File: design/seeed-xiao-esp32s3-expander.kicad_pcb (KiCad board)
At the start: 2 copper layers, 17.8 x 21.4 mm, 15 parts, among them J1 Header 1x7 2.54mm, J2 Header 1x7 2.54mm, J3 30pin, K1 TS-1185E, U1 Wio-SX1262

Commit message: Update pcb from schematic
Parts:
- removed C1: 100nF, Capacitor:C0402
- removed D1: Green, Diode:LED-0603
- removed J2: Header 1x7 2.54mm, Connector:H7-2.54
- removed K1: TS-1185E, Switch:BUTTON2P_3_9X3X2MM
- removed R1, R3: 10K, Resistor:R0402
- removed R2: 330R, Resistor:R0402
- removed R4, R5, R6, R7: 47R, Resistor:R0402
- removed TP1: Test Point, Misc:TP-D3_5c2_2mm
- removed U1: Wio-SX1262, Module:MODULE12P-1.27-11X11.6MM
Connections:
- J1 pad 1: LORA_DIO1 -> GPIO14
- J1 pad 2: LORA_BUSY -> GPIO15
- J1 pad 3: LORA_RST -> GPIO16
- J1 pad 4: LORA_SPI_NSS -> GPIO17
- J1 pad 5: LORA_RF_SW1 -> GPIO18
- J1 pad 6: unconnected-(J1-Pad6) -> GPIO47
- J1 pad 7: unconnected-(J1-Pad7) -> GPIO48
- J3 pad 10: LORA_SPI_MOSI -> unconnected-(J3-Pad10)
- J3 pad 11: LORA_BUSY -> unconnected-(J3-Pad11)
- J3 pad 13: LORA_DIO1 -> unconnected-(J3-Pad13)
- J3 pad 15: LORA_RF_SW1 -> unconnected-(J3-Pad15)
- J3 pad 6: LORA_SPI_SCK -> unconnected-(J3-Pad6)
- J3 pad 7: LORA_RST -> unconnected-(J3-Pad7)
- J3 pad 8: LORA_SPI_MISO -> unconnected-(J3-Pad8)
- J3 pad 9: LORA_SPI_NSS -> unconnected-(J3-Pad9)
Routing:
- net (no net): track 0.00 -> 136.0 mm, vias 0 -> 4
- net LORA_RST: track 29.9 -> 0.00 mm, vias 2 -> 0
- net LORA_DIO1: track 25.5 -> 0.00 mm, vias 1 -> 0
- net unconnected-(J3-Pad8): track 0.00 -> 23.6 mm, vias 0 -> 1
- net LORA_SPI_MISO: track 23.6 -> 0.00 mm, vias 1 -> 0
- net LORA_BUSY: track 23.2 -> 0.00 mm, vias 1 -> 0
- net unconnected-(J3-Pad10): track 0.00 -> 20.6 mm, vias 0 -> 1
- net LORA_SPI_MOSI: track 20.6 -> 0.00 mm, vias 1 -> 0
- net unconnected-(J3-Pad6): track 0.00 -> 20.4 mm, vias 0 -> 2
- net LORA_SPI_SCK: track 20.4 -> 0.00 mm, vias 2 -> 0
- net LORA_SPI_NSS: track 19.7 -> 0.00 mm, vias 3 -> 0
- net LORA_RF_SW1: track 19.2 -> 0.00 mm, vias 1 -> 0
- net Net-(U1-NSS): track 4.43 -> 0.00 mm, vias 1 -> 0
- net Net-(U1-MISO): track 4.33 -> 0.00 mm, vias 1 -> 0
- net Net-(U1-MOSI): track 4.27 -> 0.00 mm, vias 1 -> 0
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
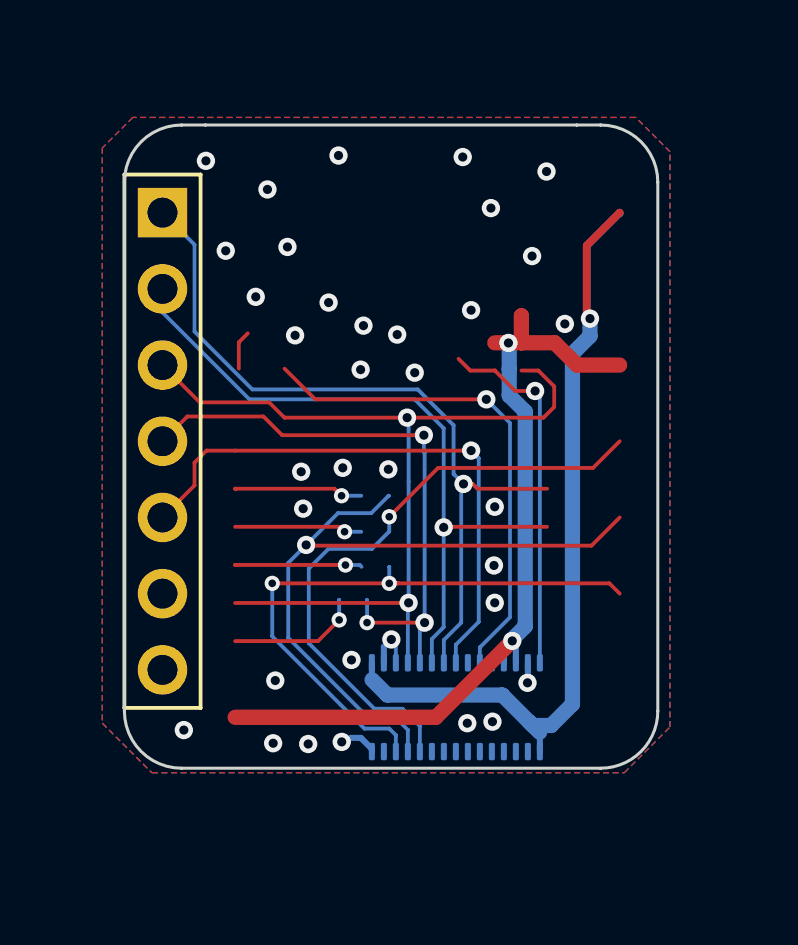
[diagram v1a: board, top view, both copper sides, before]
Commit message: Clean up traces and vias
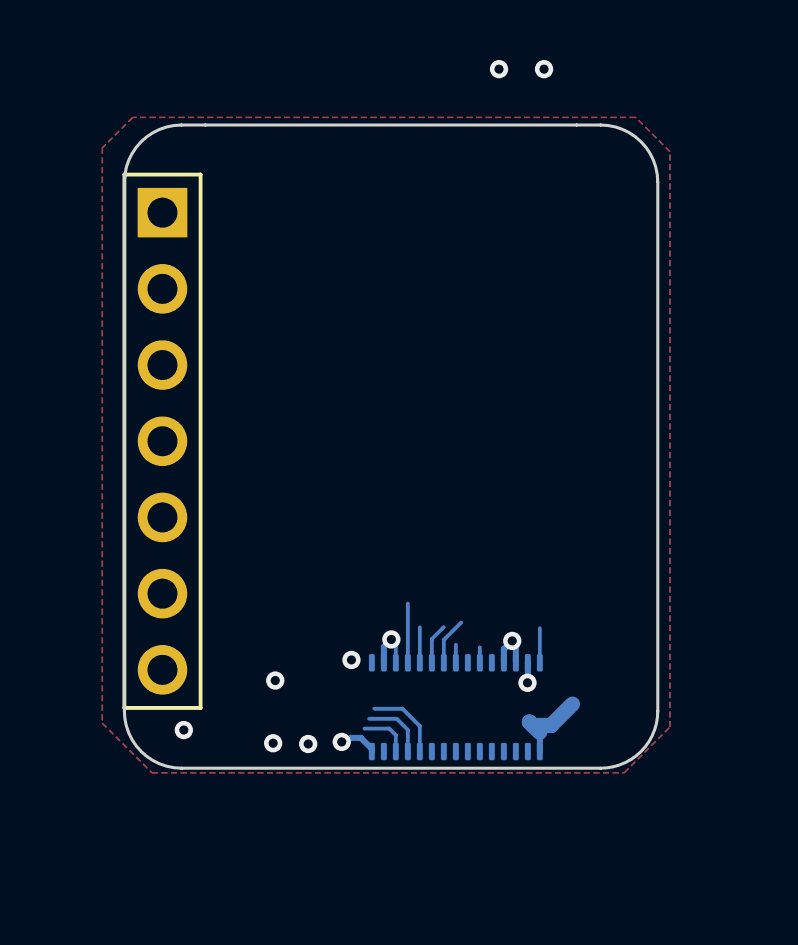
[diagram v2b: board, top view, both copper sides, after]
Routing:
- net (no net): track 136.0 -> 0.00 mm, vias 4 -> 0
- net VIN: track 30.5 -> 2.91 mm, vias 1 -> 0
- net +3V3: track 27.6 -> 1.62 mm, vias 2 -> 1
- net unconnected-(J3-Pad8): track 23.6 -> 2.17 mm, vias 1 -> 0
- net unconnected-(J3-Pad6): track 20.4 -> 1.68 mm, vias 2 -> 0
- net unconnected-(J3-Pad10): track 20.6 -> 2.61 mm, vias 1 -> 0
- net GPIO48: track 16.7 -> 0.51 mm, vias 1 -> 0
- net GPIO21: track 12.1 -> 1.15 mm, vias 1 -> 0
- net unconnected-(J3-Pad7): track 0.00 -> 1.97 mm, vias 2 -> 0
- net unconnected-(J3-Pad13): track 0.00 -> 1.58 mm, vias 1 -> 0
- net unconnected-(J3-Pad11): track 0.00 -> 1.35 mm, vias 1 -> 0
- net unconnected-(J3-Pad9): track 0.00 -> 1.18 mm, vias 3 -> 0
- net unconnected-(J3-Pad15): track 0.00 -> 0.60 mm, vias 1 -> 0
- net GND: vias 35 -> 10

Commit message: Arrange breakout holes and pads
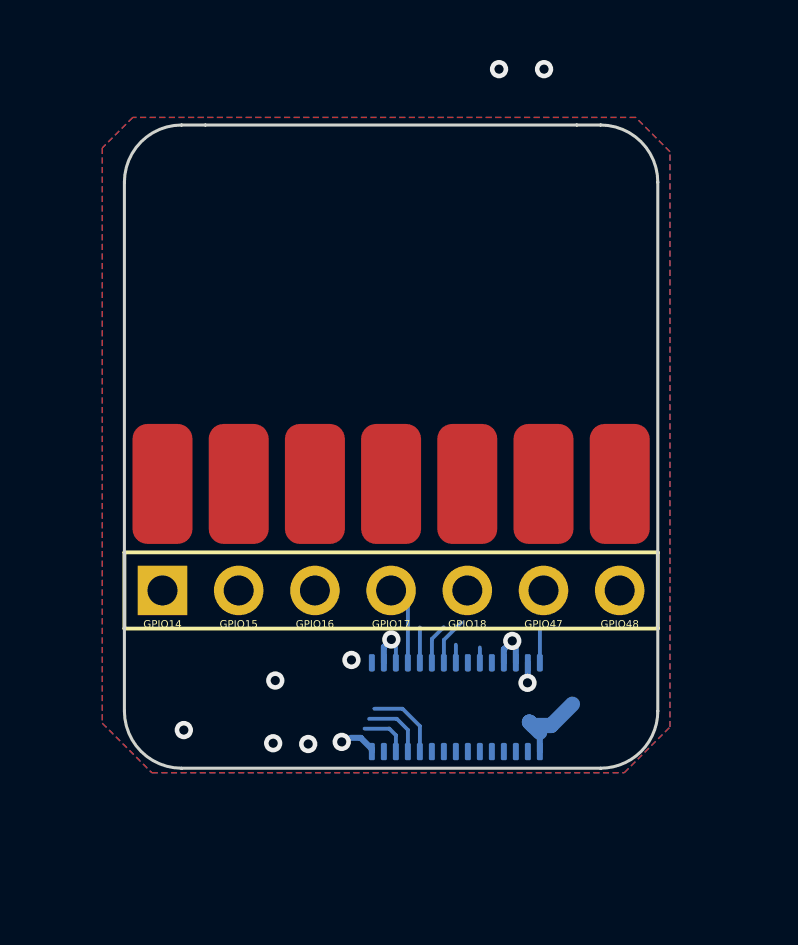
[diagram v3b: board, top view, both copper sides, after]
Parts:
- added GPIO14: SolderWirePad_1x01_SMD_2x4mm, Connector_Wire:SolderWirePad_1x01_SMD_2x4mm, F.Cu at (106.8, 122.3)
- added GPIO15: SolderWirePad_1x01_SMD_2x4mm, Connector_Wire:SolderWirePad_1x01_SMD_2x4mm, F.Cu at (109.3, 122.3)
- added GPIO16: SolderWirePad_1x01_SMD_2x4mm, Connector_Wire:SolderWirePad_1x01_SMD_2x4mm, F.Cu at (111.9, 122.3)
- added GPIO17: SolderWirePad_1x01_SMD_2x4mm, Connector_Wire:SolderWirePad_1x01_SMD_2x4mm, F.Cu at (114.4, 122.3)
- added GPIO18: SolderWirePad_1x01_SMD_2x4mm, Connector_Wire:SolderWirePad_1x01_SMD_2x4mm, F.Cu at (116.9, 122.3)
- added GPIO47: SolderWirePad_1x01_SMD_2x4mm, Connector_Wire:SolderWirePad_1x01_SMD_2x4mm, F.Cu at (119.5, 122.3)
- added GPIO48: SolderWirePad_1x01_SMD_2x4mm, Connector_Wire:SolderWirePad_1x01_SMD_2x4mm, F.Cu at (122.0, 122.3)
- moved J1 9.10 mm to (114.4, 125.9), turned to 90 degrees

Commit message: Add shared footprint for solder pad
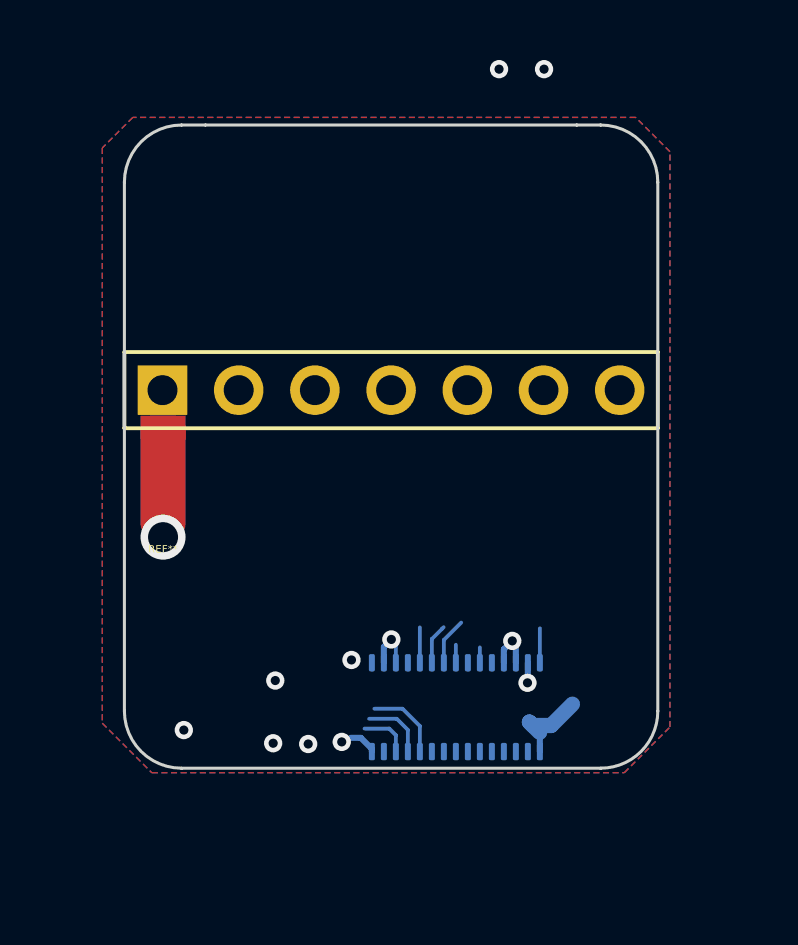
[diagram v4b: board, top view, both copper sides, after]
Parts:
- removed GPIO14, GPIO15, GPIO16, GPIO17, GPIO18, GPIO47, GPIO48: SolderWirePad_1x01_SMD_2x4mm, Connector_Wire:SolderWirePad_1x01_SMD_2x4mm
- added REF**: SolderPad_1x01_SMD, seeed-xiao-esp32s3-expander:SolderPad_1x01_SMD, F.Cu at (106.8, 122.0)
- moved J1 6.68 mm to (114.4, 119.2)
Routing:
- net unconnected-(J3-Pad7): track 1.97 -> 0.00 mm
- net GPIO14: vias 0 -> 1

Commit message: Add more organized header pad combo
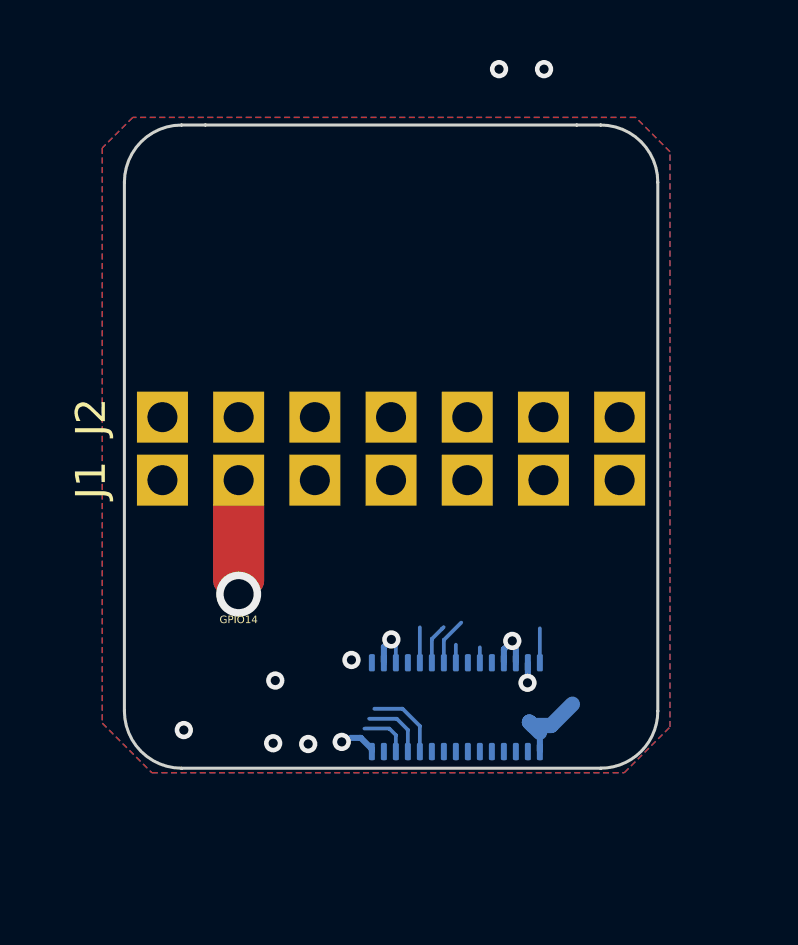
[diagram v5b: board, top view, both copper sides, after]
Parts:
- removed REF**: SolderPad_1x01_SMD, seeed-xiao-esp32s3-expander:SolderPad_1x01_SMD
- added GPIO14: SolderPad_1x01_SMD, seeed-xiao-esp32s3-expander:SolderPad_1x01_SMD, F.Cu at (109.3, 124.7)
- added J2: Conn_01x07_Pin, seeed-xiao-esp32s3-expander:PinHeader_1x07_P2.54mm, F.Cu at (106.8, 120.1)
- J1: value Header 1x7 2.54mm -> Conn_01x07_Pin; footprint Connector:H7-2.54 -> seeed-xiao-esp32s3-expander:PinHeader_1x07_P2.54mm
- moved J1 8.19 mm to (106.8, 122.2)
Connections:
- J1 pad 1: GPIO14 -> GND
- J1 pad 2: GPIO15 -> GPIO14
- J1 pad 3: GPIO16 -> GPIO15
- J1 pad 4: GPIO17 -> GPIO16
- J1 pad 5: GPIO18 -> GPIO17
- J1 pad 6: GPIO47 -> GPIO18
- J1 pad 7: GPIO48 -> GPIO21

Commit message: Add remaining gpio and pads
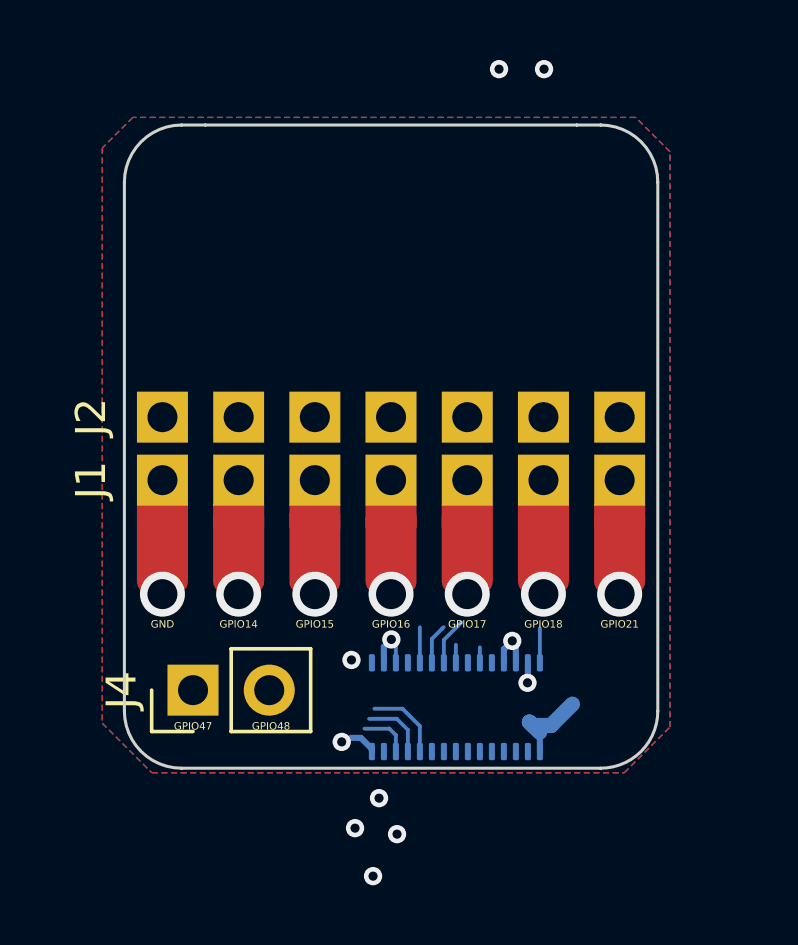
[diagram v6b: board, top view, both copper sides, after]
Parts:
- added GND: SolderPad_1x01_SMD, seeed-xiao-esp32s3-expander:SolderPad_1x01_SMD, F.Cu at (106.8, 124.7)
- added GPIO15: SolderPad_1x01_SMD, seeed-xiao-esp32s3-expander:SolderPad_1x01_SMD, F.Cu at (111.9, 124.7)
- added GPIO16: SolderPad_1x01_SMD, seeed-xiao-esp32s3-expander:SolderPad_1x01_SMD, F.Cu at (114.4, 124.7)
- added GPIO17: SolderPad_1x01_SMD, seeed-xiao-esp32s3-expander:SolderPad_1x01_SMD, F.Cu at (116.9, 124.7)
- added GPIO18: SolderPad_1x01_SMD, seeed-xiao-esp32s3-expander:SolderPad_1x01_SMD, F.Cu at (119.5, 124.7)
- added GPIO21: SolderPad_1x01_SMD, seeed-xiao-esp32s3-expander:SolderPad_1x01_SMD, F.Cu at (122.0, 124.7)
- added J4: Conn_01x02, Connector_PinHeader_2.54mm:PinHeader_1x02_P2.54mm_Vertical, F.Cu at (107.8, 129.2)
- J1, J2: value Conn_01x07_Pin -> Conn_01x07
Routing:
- net GPIO21: vias 0 -> 1
- net GPIO18: vias 0 -> 1
- net GPIO17: vias 0 -> 1
- net GPIO16: vias 0 -> 1
- net GPIO15: vias 0 -> 1
- net GND: vias 10 -> 11
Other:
- board text added: "GPIO47"
- board text added: "GPIO48"

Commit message: Add VIN pin
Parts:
- added J5: Conn_01x01, Connector_PinHeader_2.54mm:PinHeader_1x01_P2.54mm_Vertical, F.Cu at (122.0, 129.4)
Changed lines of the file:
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@@
 		(embedded_fonts no)
 	)
+	(footprint "Connector_PinHeader_2.54mm:PinHeader_1x01_P2.54mm_Vertical"
+		(layer "F.Cu")
+		(at 121.995 129.395)
+		(descr "Through hole straight pin header, 1x01, 2.54mm pitch, single row")
+		(tags "Through hole pin header THT 1x01 2.54mm single row")
+		(property "Reference" "J5"
+			(at 2.805 0.005 0)
+			(layer "F.SilkS")
+			(effects
+				(font
+					(size 1 1)
+					(thickness 0.15)
+				)
+			)
+		)
+		(property "Value" "Conn_01x01"
+			(at 0 2.38 0)
+			(layer "F.Fab")
+			(effects
+				(font
+					(size 1 1)
+					(thickness 0.15)
+				)
+			)
+		)
+		(property "Datasheet" ""
+			(at 0 0 0)
+			(layer "F.Fab")
+			(hide yes)
+			(effects
+				(font
+					(size 1.27 1.27)
+				)
+			)
+		)
+		(property "Description" "Generic connector, single row, 01x01, script generated (kicad-library-utils/schlib/autogen/connector/)"
+			(at 0 0 0)
+			(layer "F.Fab")
+			(hide yes)
+			(effects
+				(font
+					(size 1.27 1.27)
+				)
+			)
+		)
+		(property ki_fp_filters "Connector*:*_1x??_*")
+		(sheetname "/")
+		(sheetfile "seeed-xiao-esp32s3-expander.kicad_sch")
+		(attr through_hole)
+		(duplicate_pad_numbers_are_jumpers no)
+		(fp_line
+			(start -1.38 -1.38)
+			(end 0 -1.38)
+			(stroke
+				(width 0.12)
+				(type solid)
+			)
+			(layer "F.SilkS")
+		)
+		(fp_line
+			(start -1.38 0)
+			(end -1.38 -1.38)
+			(stroke
+				(width 0.12)
+				(type solid)
+			)
+			(layer "F.SilkS")
+		)
+		(fp_line
+			(start -1.38 1.27)
+			(end -1.38 1.38)
+			(stroke
+				(width 0.12)
+				(type solid)
+			)
+			(layer "F.SilkS")
+		)
+		(fp_line
+			(start 1.38 1.27)
+			(end 1.38 1.38)
+			(stroke
+				(width 0.12)
+				(type solid)
+			)
+			(layer "F.SilkS")
+		)
+		(fp_rect
+			(start -1.77 -1.77)
+			(end 1.77 1.77)
+			(stroke
+				(width 0.05)
+				(type solid)
+			)
+			(fill no)
+			(layer "F.CrtYd")
+		)
+		(fp_line
+			(start -1.27 -0.635)
+			(end -0.635 -1.27)
+			(stroke
+				(width 0.1)
+				(type solid)
+			)
+			(layer "F.Fab")
+		)
+		(fp_line
+			(start -1.27 1.27)
+			(end -1.27 -0.635)
+			(stroke
+				(width 0.1)
+				(type solid)
+			)
+			(layer "F.Fab")
+		)
+		(fp_line
+			(start -0.635 -1.27)
+			(end 1.27 -1.27)
+			(stroke
+				(width 0.1)
+				(type solid)
+			)
+			(layer "F.Fab")
+		)
+		(fp_line
+			(start 1.27 -1.27)
+			(end 1.27 1.27)
+			(stroke
+				(width 0.1)
+				(type solid)
+			)
+			(layer "F.Fab")
+		)
+		(fp_line
+			(start 1.27 1.27)
+			(end -1.27 1.27)
+			(stroke
+				(width 0.1)
+				(type solid)
+			)
+			(layer "F.Fab")
+		)
+		(fp_text user "${REFERENCE}"
+			(at 0 0 90)
+			(layer "F.Fab")
+			(effects
+				(font
+					(size 1 1)
+					(thickness 0.15)
+				)
+			)
+		)
+		(pad "1" thru_hole rect
+			(at 0 0)
+			(size 1.7 1.7)
+			(drill 1)
+			(layers "*.Cu" "*.Mask")
+			(remove_unused_layers no)
+			(net "VIN")
+			(pinfunction "Pin_1_1")
+			(pintype "passive")
+		)
+		(embedded_fonts no)
+		(model "${KICAD10_3DMODEL_DIR}/Connector_PinHeader_2.54mm.3dshapes/PinHeader_1x01_P2.54mm_Vertical.step"
+			(hide yes)
+			(offset
+				(xyz 0 0 0)
+			)
+			(scale
+				(xyz 1 1 1)
+			)
+			(rotate
+				(xyz 0 0 0)
+			)
+		)
+	)
 	(footprint "Connector_PinHeader_2.54mm:PinHeader_1x02_P2.54mm_Vertical"
 		(layer "F.Cu")
@@
 		(tags "Through hole pin header THT 1x02 2.54mm single row")
 		(property "Reference" "J4"
-			(at 0 -2.38 90)
+			(at 0 -3 90)
 			(layer "F.SilkS")
 			(effects
@@
 		)
 	)
+	(gr_text "VIN\n"
+		(at 122 130.6 0)
+		(layer "F.SilkS")
+		(effects
+			(font
+				(size 0.25 0.25)
+				(thickness 0.0625)
+			)
+		)
+	)
 	(gr_text "Wio-SX1262 for XIAO V1.1\n"
 		(at 117.2464 111.4298 90)
@@
 	)
 	(via
-		(at 109.32 126)
-		(size 1.5)
-		(drill 1)
-		(layers "F.Cu" "B.Cu")
-		(locked yes)
-		(net "GPIO14")
-	)
-	(via
-		(at 111.86 126)
-		(size 1.5)
-		(drill 1)
-		(layers "F.Cu" "B.Cu")
-		(locked yes)
-		(net "GPIO15")
-	)
-	(via
 		(at 114.4 126)
 		(size 1.5)
@@
 		(net "GPIO16")
 	)
+	(segment
+		(start 117.360598 127.774802)
+		(end 117.360598 128.28809)
+		(width 0.127)
+		(layer "B.Cu")
+		(net "GPIO48")
+	)
 	(via
 		(at 116.94 126)
@@
 	)
 	(via
-		(at 119.48 126)
-		(size 1.5)
-		(drill 1)
-		(layers "F.Cu" "B.Cu")
-		(locked yes)
-		(net "GPIO18")
-	)
-	(via
-		(at 122.02 126)
+		(at 111.86 126)
 		(size 1.5)
 		(drill 1)
 		(layers "F.Cu" "B.Cu")
 		(locked yes)
-		(net "GPIO21")
-	)
-	(segment
-		(start 119.360598 127.139402)
-		(end 119.360598 128.28809)
-		(width 0.127)
-		(layer "B.Cu")
-		(net "GPIO21")
+		(net "GPIO15")
 	)
 	(via
@@
 		(net "GND")
 	)
+	(via
+		(at 119.48 126)
+		(size 1.5)
+		(drill 1)
+		(layers "F.Cu" "B.Cu")
+		(locked yes)
+		(net "GPIO18")
+	)
+	(via
+		(at 122.02 126)
+		(size 1.5)
+		(drill 1)
+		(layers "F.Cu" "B.Cu")
+		(locked yes)
+		(net "GPIO21")
+	)
+	(segment
+		(start 119.360598 127.139402)
+		(end 119.360598 128.28809)
+		(width 0.127)
+		(layer "B.Cu")
+		(net "GPIO21")
+	)
+	(via
+		(at 109.32 126)
+		(size 1.5)
+		(drill 1)
+		(layers "F.Cu" "B.Cu")
+		(locked yes)
+		(net "GPIO14")
+	)
 	(segment
 		(start 119.360598 130.612798)
@@
 		(net "unconnected-(J3-Pad15)")
 	)
-	(segment
-		(start 117.360598 127.774802)
-		(end 117.360598 128.28809)
-		(width 0.127)
-		(layer "B.Cu")
-		(net "GPIO48")
-	)
 	(via
